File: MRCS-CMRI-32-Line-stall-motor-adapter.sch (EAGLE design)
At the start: 4 parts

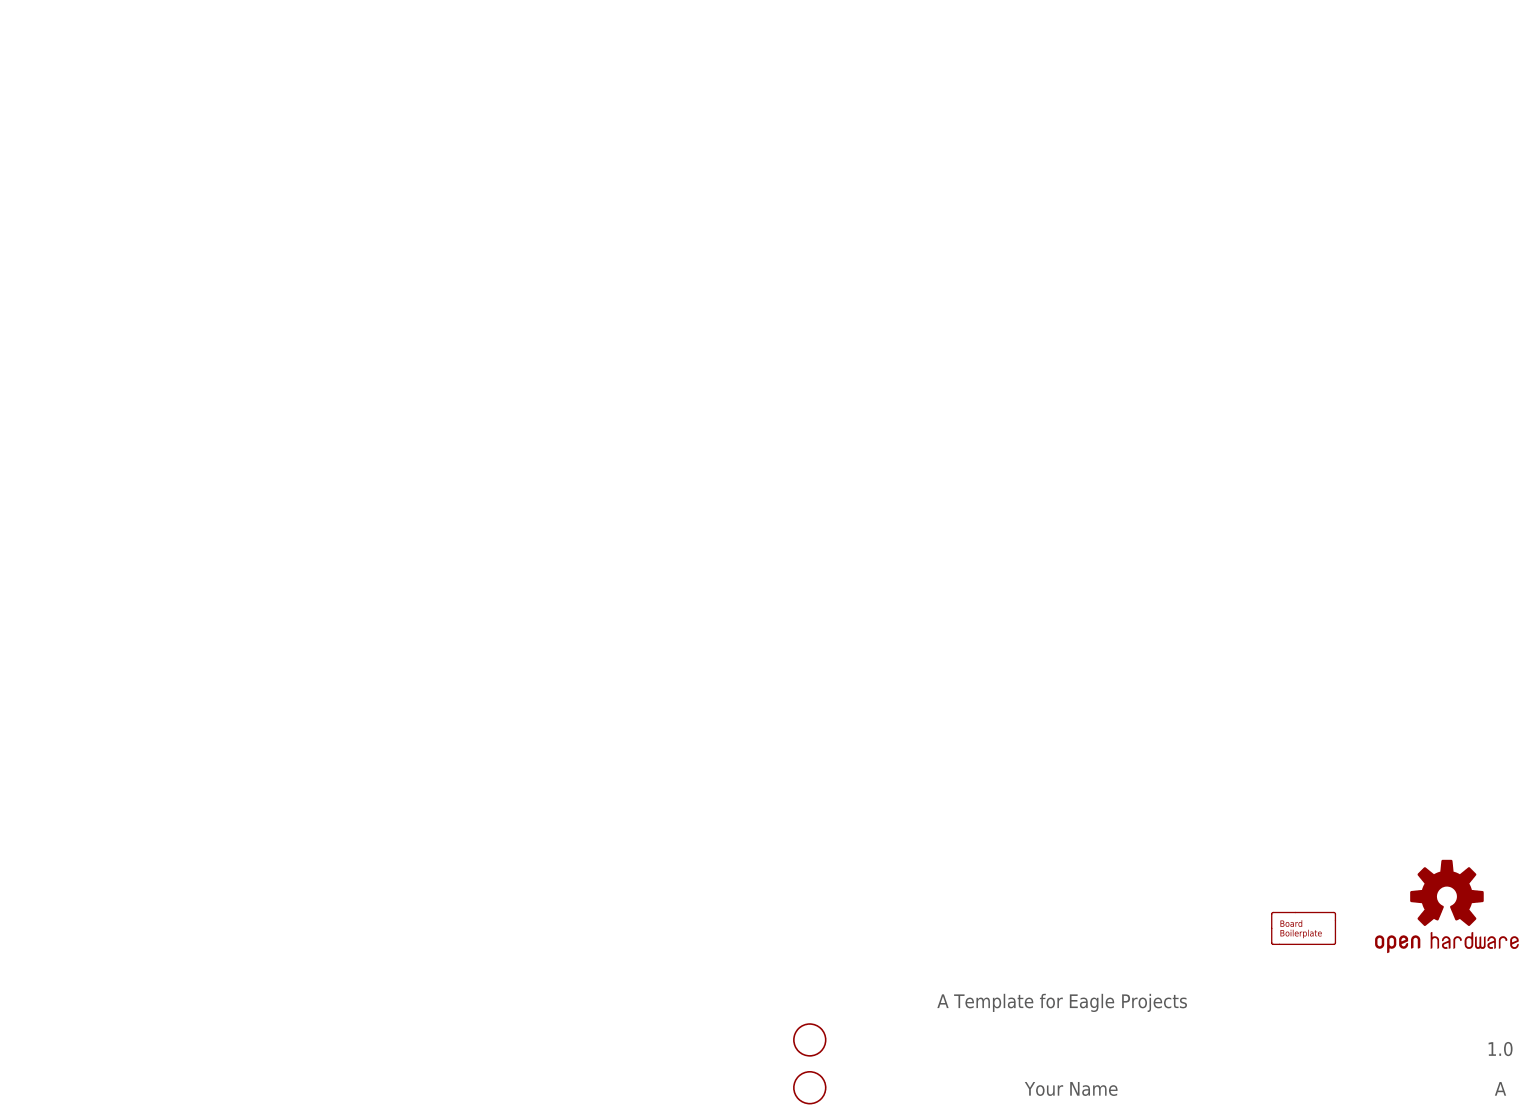
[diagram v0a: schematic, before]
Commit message: clean up at end of Version 1.0
made pdfs of Schematic and layout, cleaned up work files.  This version passes all electrical design rules and created a believable set of gerbers
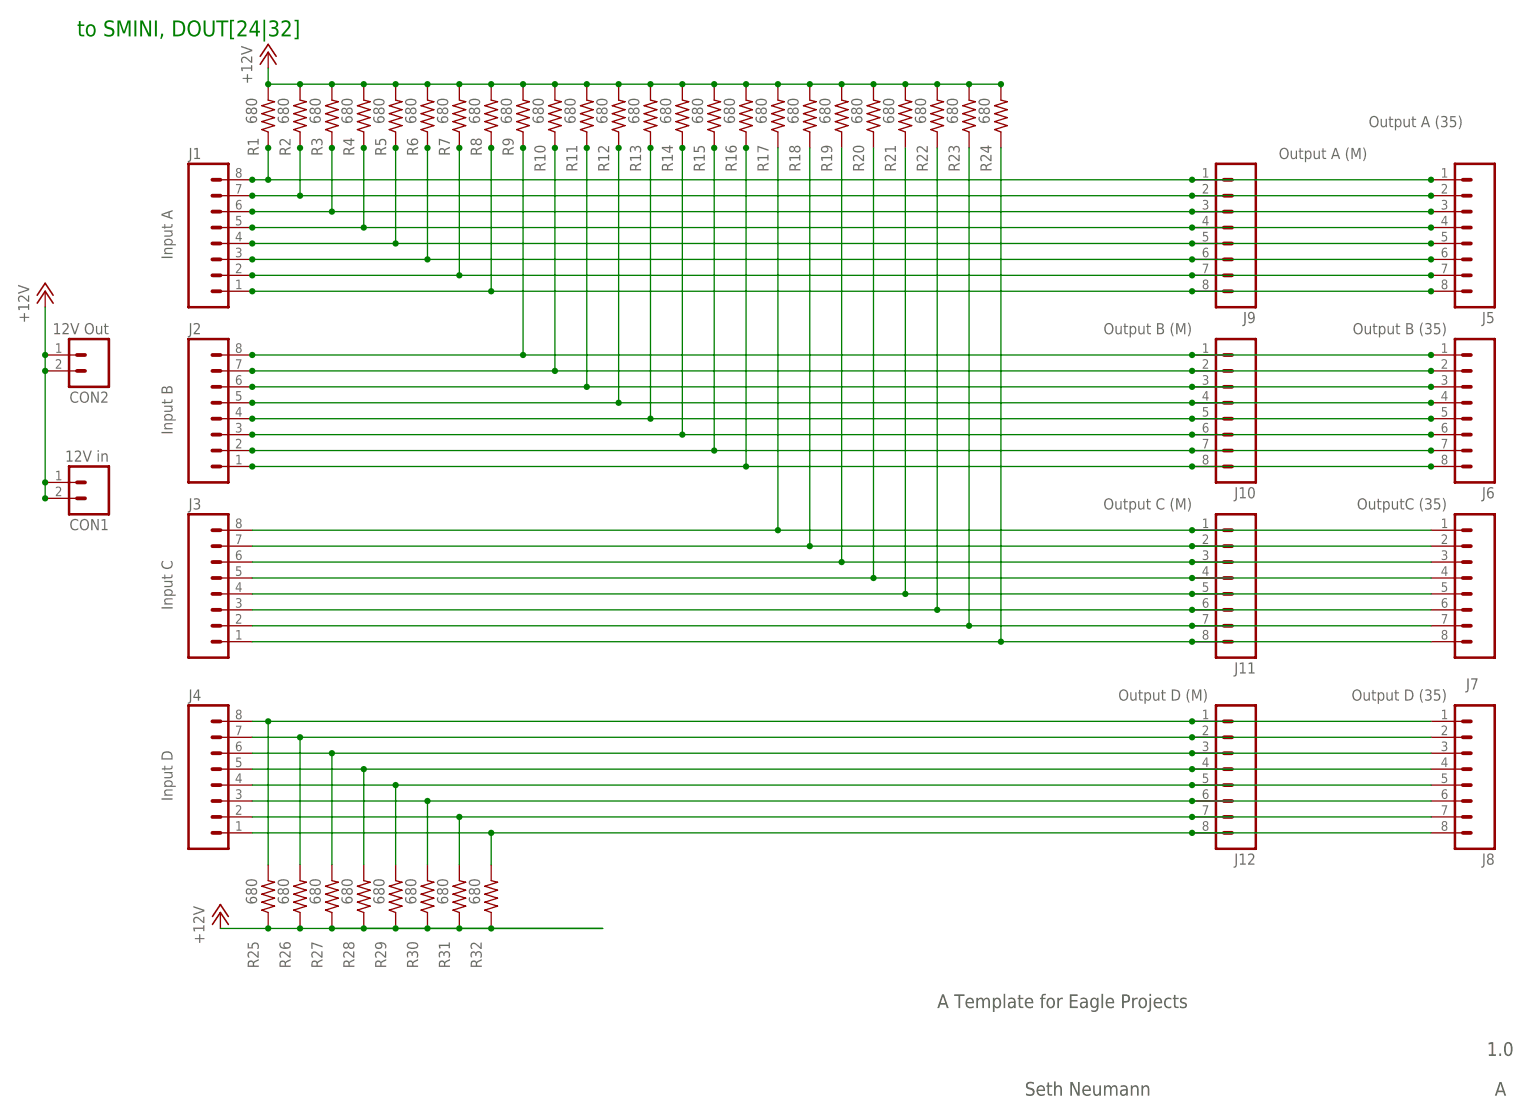
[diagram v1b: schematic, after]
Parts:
- removed BOARD1: BOARD80X100, SPCoast:BOARD80X100
- removed FID1, FID2: FIDUCIAL, SPCoast:FIDUCIAL
- removed OSHW1: DOC-OSHW-LOGO-M, SPCoast:DOC-OSHW-LOGO-M
- added CON1: 12V in, SPCoast:CONNECTOR-M025MM-LOCK
- added CON2: 12V Out, SPCoast:CONNECTOR-M025MM-LOCK
- added J1: Input A, SPCoast:CONNECTOR-M081.56-F
- added J10: Output B (M), SPCoast:CONNECTOR-M081.56-F
- added J11: Output C (M), SPCoast:CONNECTOR-M081.56-F
- added J12: Output D (M), SPCoast:CONNECTOR-M081.56-F
- added J2: Input B, SPCoast:CONNECTOR-M081.56-F
- added J3: Input C, SPCoast:CONNECTOR-M081.56-F
- added J4: Input D, SPCoast:CONNECTOR-M081.56-F
- added J5: Output A (35), SPCoast:CONNECTOR-M083.5MM-8
- added J6: Output B (35), SPCoast:CONNECTOR-M083.5MM-8
- added J7: OutputC (35), SPCoast:CONNECTOR-M083.5MM-8
- added J8: Output D (35), SPCoast:CONNECTOR-M083.5MM-8
- added J9: Output A (M), SPCoast:CONNECTOR-M081.56-F
- added R1, R10, R11, R12, R13, R14, R15, R16, R17, R18, R19, R2, R20, R21, R22, R23, R24, R25, R26, R27, R28, R29, R3, R30, R31, R32, R4, R5, R6, R7, R8, R9: 680, SparkFun-Passives:RESISTORPTH-1/2W
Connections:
- new net +12V: CON1.A, CON1.B, CON2.A, CON2.B, R1.2, R10.2, R11.2, R12.2, R13.2, R14.2, R15.2, R16.2, R17.2, R18.2, R19.2, R2.2, R20.2, R21.2, R22.2, R23.2, R24.2, R25.1, R26.1, R27.1, R28.1, R29.1, R3.2, R30.1, R31.1, R32.1, R4.2, R5.2, R6.2, R7.2, R8.2, R9.2
- new net N$1: J1.5, J5.4, J9.4, R4.1
- new net N$10: J1.3, J5.6, J9.6, R6.1
- new net N$11: J1.2, J5.7, J9.7, R7.1
- new net N$12: J1.1, J5.8, J9.8, R8.1
- new net N$13: J1.6, J5.3, J9.3, R3.1
- new net N$14: J10.2, J2.7, J6.2, R10.1
- new net N$15: J10.7, J2.2, J6.7, R15.1
- new net N$16: J10.8, J2.1, J6.8, R16.1
- new net N$17: J10.4, J2.5, J6.4, R12.1
- new net N$18: J11.2, J3.7, J7.2, R18.1
- new net N$19: J11.3, J3.6, J7.3, R19.1
- new net N$2: J1.8, J5.1, J9.1, R1.1
- new net N$20: J11.4, J3.5, J7.4, R20.1
- new net N$21: J11.5, J3.4, J7.5, R21.1
- new net N$22: J11.6, J3.3, J7.6, R22.1
- new net N$23: J11.7, J3.2, J7.7, R23.1
- new net N$24: J11.8, J3.1, J7.8, R24.1
- new net N$25: J12.1, J4.8, J8.1, R25.2
- new net N$26: J12.2, J4.7, J8.2, R26.2
- new net N$27: J12.3, J4.6, J8.3, R27.2
- new net N$28: J12.4, J4.5, J8.4, R28.2
- new net N$29: J12.5, J4.4, J8.5, R29.2
- new net N$3: J10.1, J2.8, J6.1, R9.1
- new net N$30: J12.6, J4.3, J8.6, R30.2
- new net N$31: J12.7, J4.2, J8.7, R31.2
- new net N$32: J12.8, J4.1, J8.8, R32.2
- new net N$4: J1.7, J5.2, J9.2, R2.1
- new net N$5: J10.3, J2.6, J6.3, R11.1
- new net N$6: J11.1, J3.8, J7.1, R17.1
- new net N$7: J10.5, J2.4, J6.5, R13.1
- new net N$8: J10.6, J2.3, J6.6, R14.1
- new net N$9: J1.4, J5.5, J9.5, R5.1
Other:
- note added: "Seth Neumann"
- note added: "to SMINI, DOUT[24|32]"
- note removed: "Your Name"
